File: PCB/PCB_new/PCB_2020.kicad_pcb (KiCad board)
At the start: 2 copper layers, 94 x 98.4 mm, 26 parts, among them IC1 LM358N, J10 SERVO_CONN, J11 MC_CONN, Q1 220mA/50V/3.5Ω, Q2 100V/17A, Q3 100V/17A, Q4 100V/17A, Q5 100V/17A, Q6 100V/17A, U1 TI_CONN

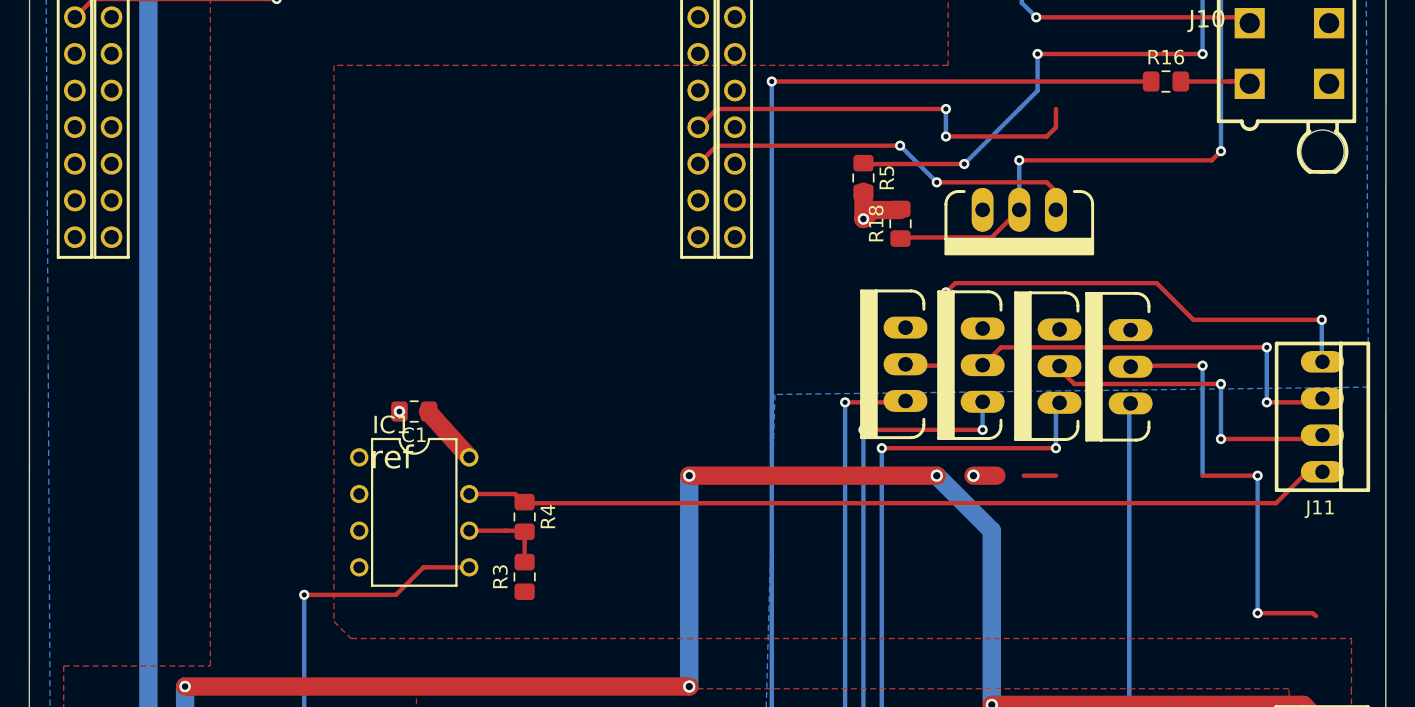
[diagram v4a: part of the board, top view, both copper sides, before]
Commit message: fixed orientation of the mosfets and other errors in pin layouts
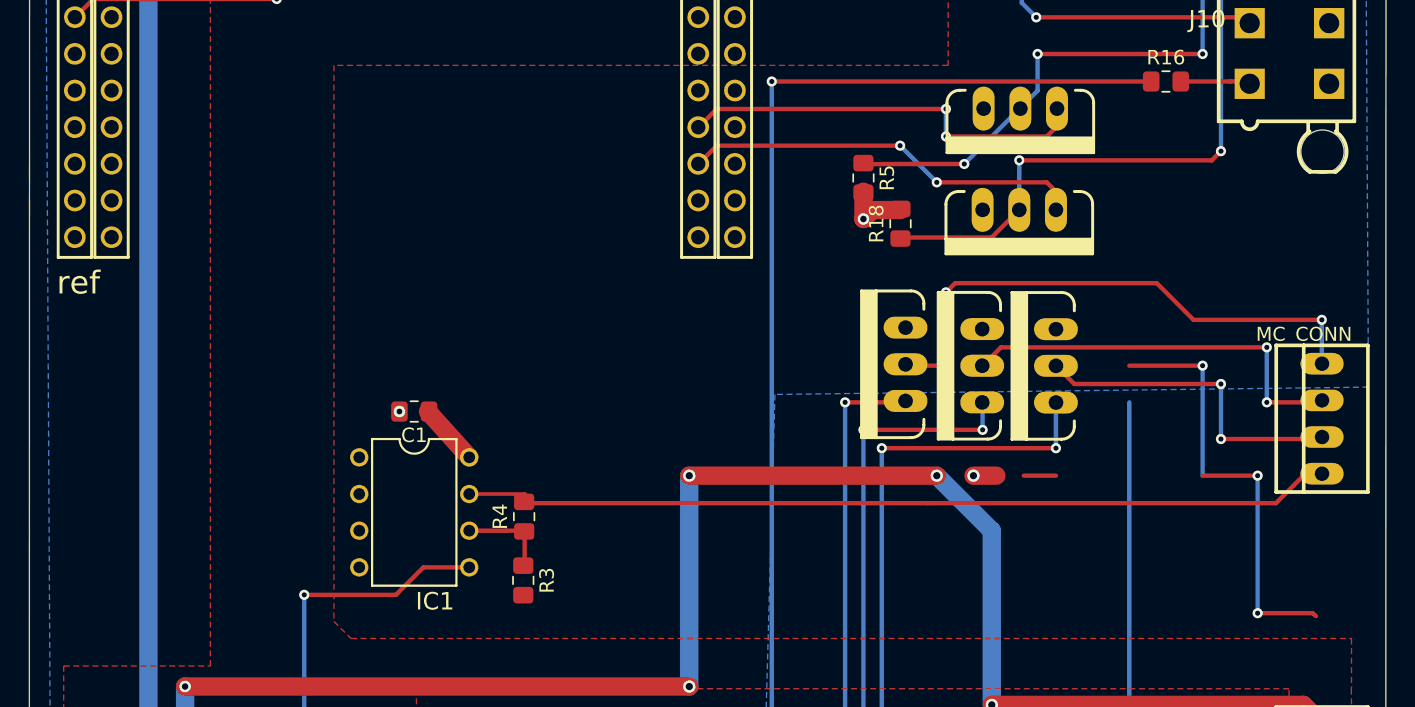
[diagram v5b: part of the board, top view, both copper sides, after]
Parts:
- moved Q3 19.4 mm to (170.2, 76.7), turned to 180 degrees
- moved Q5 5.36 mm to (167.5, 94.5)
- moved Q4 5.08 mm to (172.6, 94.5)
- moved R3 0.26 mm to (135.7, 109.4), turned to 270 degrees
- moved J11 0.13 mm to (191.1, 98.2), turned to 90 degrees
- turned R4 to 90 degrees
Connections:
- IC1 pad 1: /LAUNCHXL-F28379D Breakout/THROTTLE_MC -> (no net)
- IC1 pad 2: Net-(IC1-Pad2) -> (no net)
- IC1 pad 3: THROTTLE_DAC -> (no net)
- IC1 pad 5: +12V -> THROTTLE_DAC
- IC1 pad 6: (no net) -> Net-(IC1-Pad6)
- IC1 pad 7: (no net) -> /LAUNCHXL-F28379D Breakout/THROTTLE_MC
- IC1 pad 8: (no net) -> +12V
- Q2 pad 1: /LAUNCHXL-F28379D Breakout/INPUT_A+ -> INPUT_A+_CTL
- Q2 pad 2: INPUT_A+_CTL -> /LAUNCHXL-F28379D Breakout/INPUT_A+
- Q3 pad 1: /LAUNCHXL-F28379D Breakout/EN+ -> EN+_CTL
- Q3 pad 2: EN+_CTL -> /LAUNCHXL-F28379D Breakout/EN+
- Q4 pad 1: /LAUNCHXL-F28379D Breakout/REV_MC -> REV_CTL
- Q4 pad 2: REV_CTL -> /LAUNCHXL-F28379D Breakout/REV_MC
- Q5 pad 1: /LAUNCHXL-F28379D Breakout/FWD_MC -> FWD_CTL
- Q5 pad 2: FWD_CTL -> /LAUNCHXL-F28379D Breakout/FWD_MC
- Q6 pad 1: /LAUNCHXL-F28379D Breakout/FS1_MC -> FS1_CTL
- Q6 pad 2: FS1_CTL -> /LAUNCHXL-F28379D Breakout/FS1_MC
- R3 pad 1: Net-(IC1-Pad2) -> Net-(IC1-Pad6)
- R4 pad 1: Net-(IC1-Pad2) -> Net-(IC1-Pad6)
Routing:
- net (no net): track 0.00 -> 145.7 mm, vias 0 -> 3
- net /LAUNCHXL-F28379D Breakout/EN+: track 145.7 -> 12.7 mm, vias 3 -> 1
- net THROTTLE_DAC: track 0.00 -> 64.3 mm, vias 0 -> 2
- net +12V: track 77.1 -> 12.8 mm, vias 5 -> 3
- net THROTTLE_MC: track 60.1 -> 0.00 mm
- net REV_CTL: track 0.00 -> 58.3 mm, vias 0 -> 3
- net /LAUNCHXL-F28379D Breakout/REV_MC: track 78.5 -> 22.8 mm, vias 5 -> 2
- net /LAUNCHXL-F28379D Breakout/FWD_MC: track 81.1 -> 27.8 mm, vias 5 -> 2
- net FWD_CTL: track 0.00 -> 50.7 mm, vias 0 -> 3
- net FS1_CTL: track 0.00 -> 43.1 mm, vias 0 -> 2
- net INPUT_A+_CTL: track 0.00 -> 27.9 mm, vias 0 -> 2
- net /LAUNCHXL-F28379D Breakout/INPUT_A+: track 27.9 -> 0.00 mm, vias 2 -> 0
- net /LAUNCHXL-F28379D Breakout/THROTTLE_MC: track 38.1 -> 60.1 mm, vias 3 -> 0
- net EN+_CTL: track 41.4 -> 28.7 mm, vias 3 -> 2
- net Net-(IC1-Pad6): track 0.00 -> 6.09 mm
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
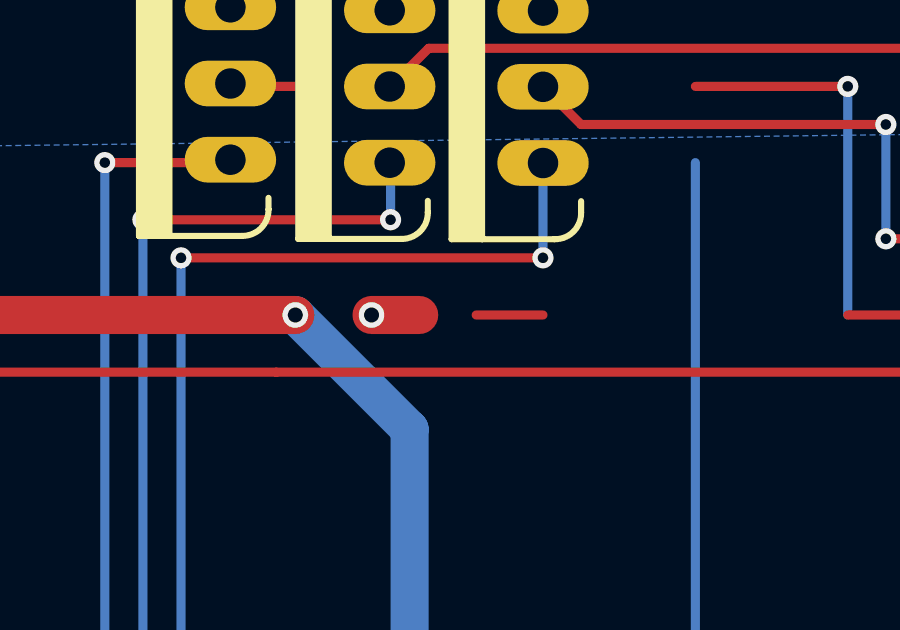
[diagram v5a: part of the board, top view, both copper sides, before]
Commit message: removed extra wires from old breaking
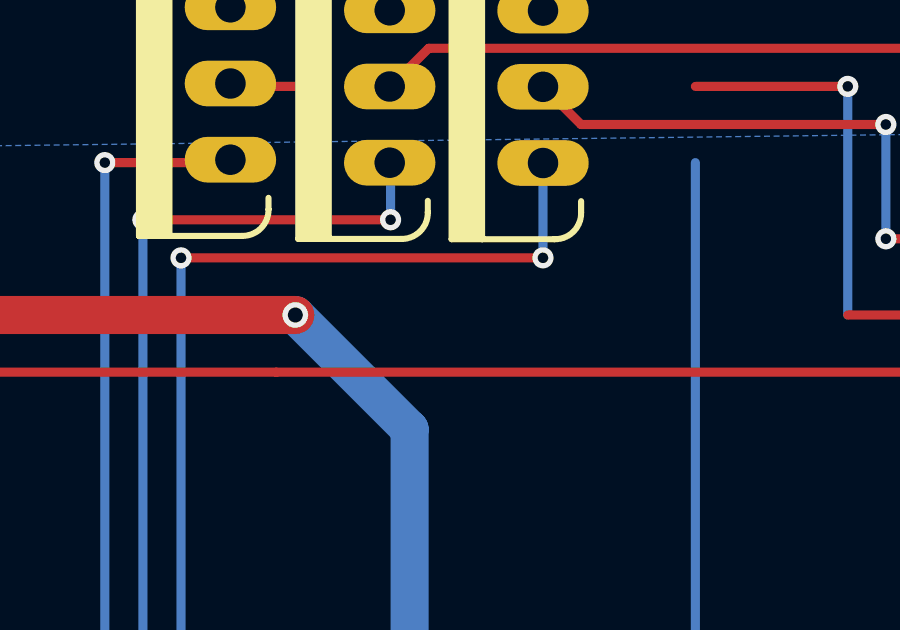
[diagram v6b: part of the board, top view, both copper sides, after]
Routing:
- net N$2: track 2.22 -> 0.00 mm
- net +12V: track 12.8 -> 11.2 mm, vias 3 -> 2

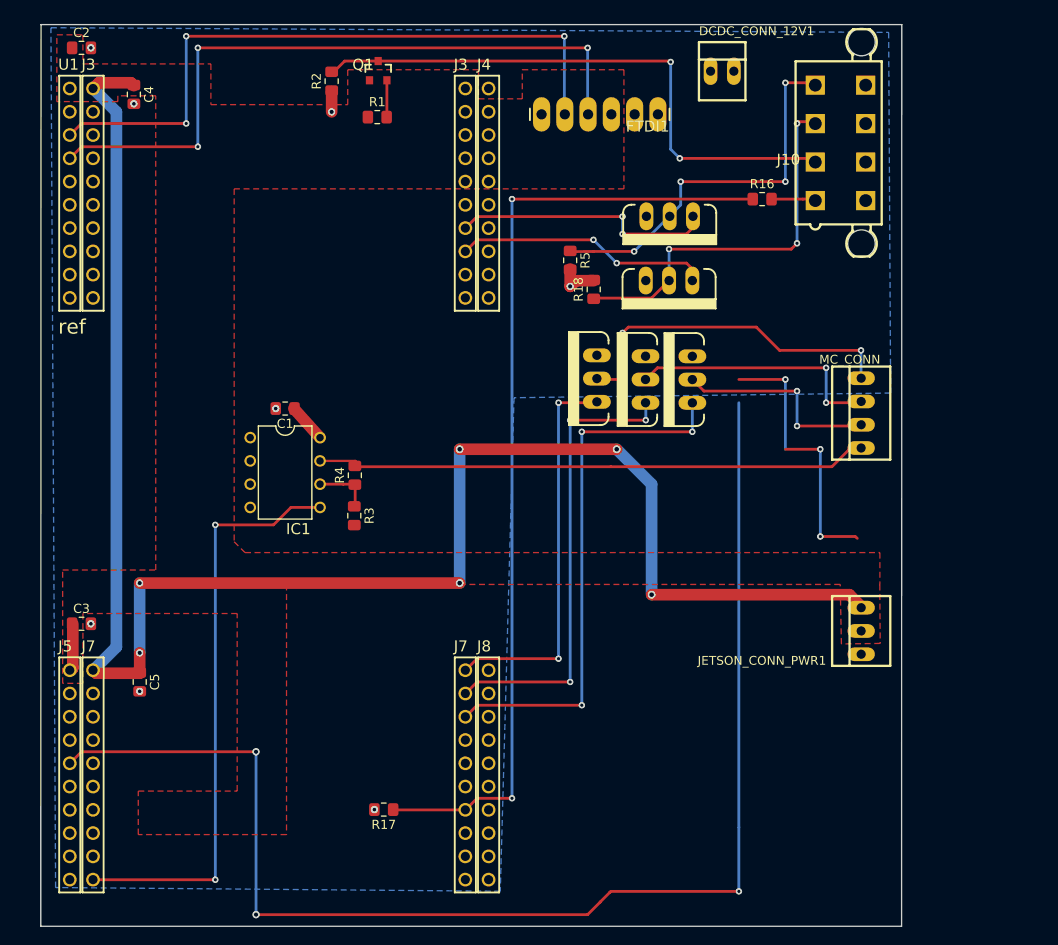
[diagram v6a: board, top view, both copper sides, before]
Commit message: routed 12V wires
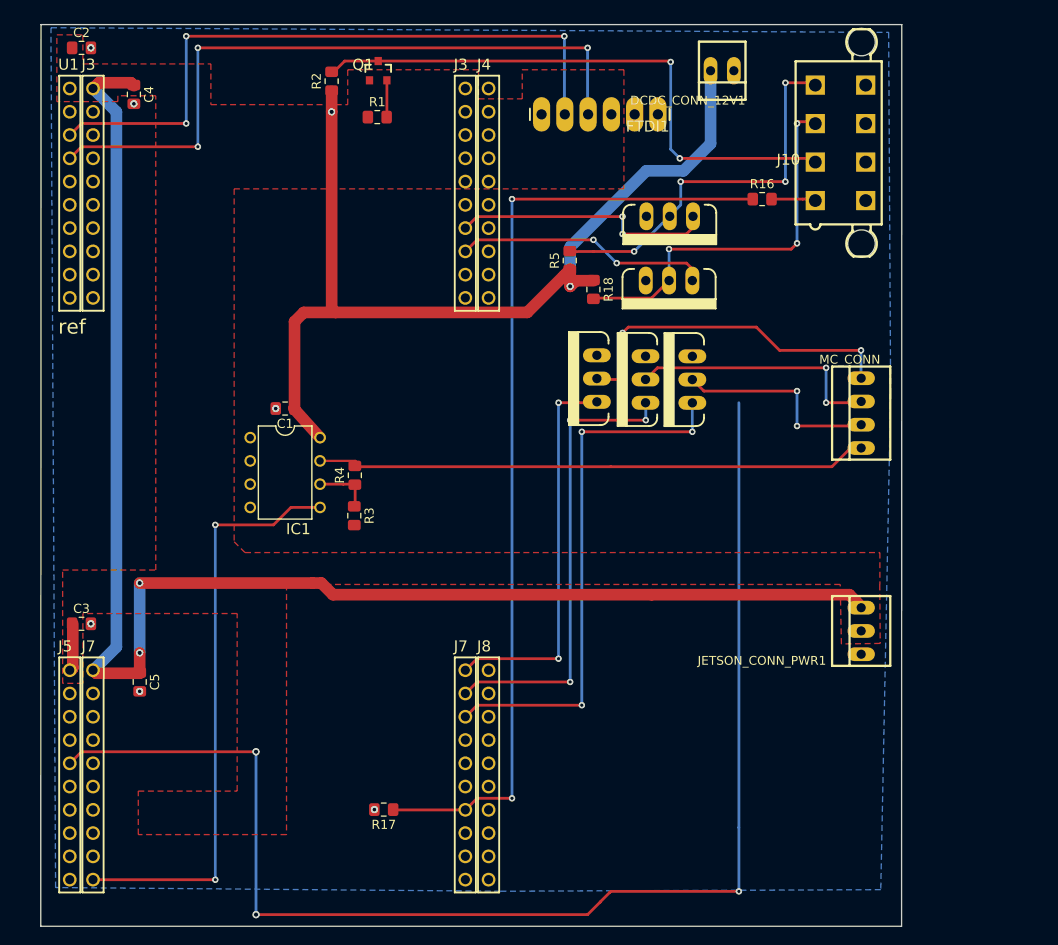
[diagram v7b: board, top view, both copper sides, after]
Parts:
- moved DCDC_CONN_12V1 0.05 mm to (175.9, 60.8), turned to 180 degrees
- turned R5 to 90 degrees
- turned R18 to 270 degrees
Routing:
- net +12V: track 11.2 -> 107.4 mm
- net EN+: track 41.9 -> 0.00 mm, vias 4 -> 0
- net INPUT_A+: track 41.5 -> 0.00 mm, vias 3 -> 0
- net /LAUNCHXL-F28379D Breakout/INPUT_A+: track 0.00 -> 41.5 mm, vias 0 -> 3
- net /LAUNCHXL-F28379D Breakout/EN+: track 12.7 -> 41.9 mm, vias 1 -> 4
- net +5V: track 193.0 -> 165.4 mm, vias 6 -> 2
- net BRAKE_SOLENOID: track 17.4 -> 0.00 mm, vias 2 -> 0

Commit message: Clean Old Design (no braking)
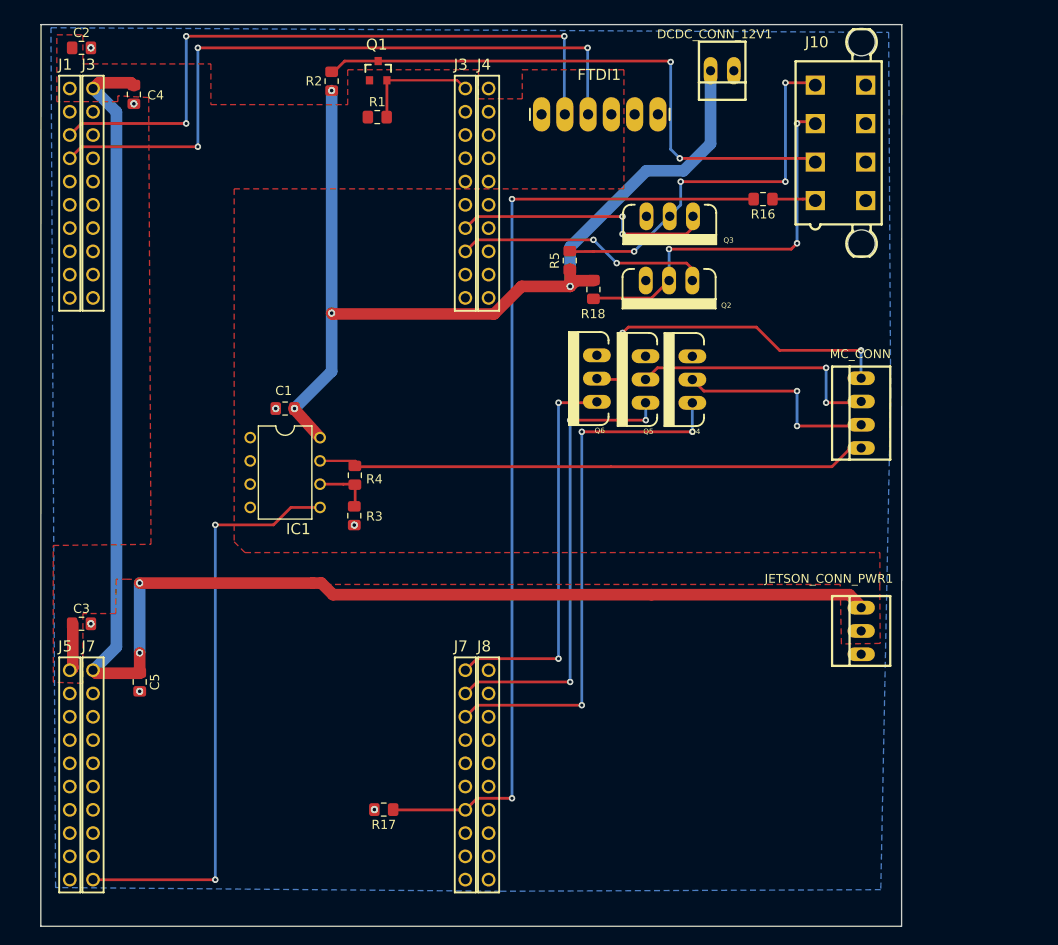
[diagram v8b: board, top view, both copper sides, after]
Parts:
- removed U1: TI_CONN, Drivetrain_control:TI_Footprint
- added J1: TI_CONN, Drivetrain_control:TI_Footprint, F.Cu at (103.5, 87.0)
- moved R16 0.10 mm to (180.3, 74.8), turned to 180 degrees
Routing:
- net (no net): track 145.7 -> 0.00 mm, vias 3 -> 0
- net TI_PWM: track 4.08 -> 13.0 mm
- net /LAUNCHXL-F28379D Breakout/HLFB+: track 0.00 -> 4.56 mm
- net MC_HLFB+: track 109.9 -> 105.3 mm
- net +12V: track 107.4 -> 105.0 mm, vias 2 -> 4
- net GND: vias 6 -> 7
